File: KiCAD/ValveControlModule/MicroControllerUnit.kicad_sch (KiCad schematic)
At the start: 5 parts, among them U1 XIAO-RP2040-DIP

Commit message: 電源，RS485の仕様を確定
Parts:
- H1, H2, H3, H4: footprint MountingHole:MountingHole_4.3mm_M4_Pad_TopBottom -> MountingHole:MountingHole_3.2mm_M3_Pad_TopBottom
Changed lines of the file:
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@@
 			)
 		)
-		(property "Footprint" "MountingHole:MountingHole_4.3mm_M4_Pad_TopBottom"
+		(property "Footprint" "MountingHole:MountingHole_3.2mm_M3_Pad_TopBottom"
 			(at 190.5 39.37 0)
 			(effects
@@
 			)
 		)
-		(property "Footprint" "MountingHole:MountingHole_4.3mm_M4_Pad_TopBottom"
+		(property "Footprint" "MountingHole:MountingHole_3.2mm_M3_Pad_TopBottom"
 			(at 114.3 39.37 0)
 			(effects
@@
 			)
 		)
-		(property "Footprint" "MountingHole:MountingHole_4.3mm_M4_Pad_TopBottom"
+		(property "Footprint" "MountingHole:MountingHole_3.2mm_M3_Pad_TopBottom"
 			(at 139.7 39.37 0)
 			(effects
@@
 			)
 		)
-		(property "Footprint" "MountingHole:MountingHole_4.3mm_M4_Pad_TopBottom"
+		(property "Footprint" "MountingHole:MountingHole_3.2mm_M3_Pad_TopBottom"
 			(at 165.1 39.37 0)
 			(effects

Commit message: 基本的な機能が完成
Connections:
- no-connect marks 0 -> 1
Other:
- note added: "内部の回路にパスコンあるため省略"
- moved on the sheet: H1, H2, H3, H4, U1

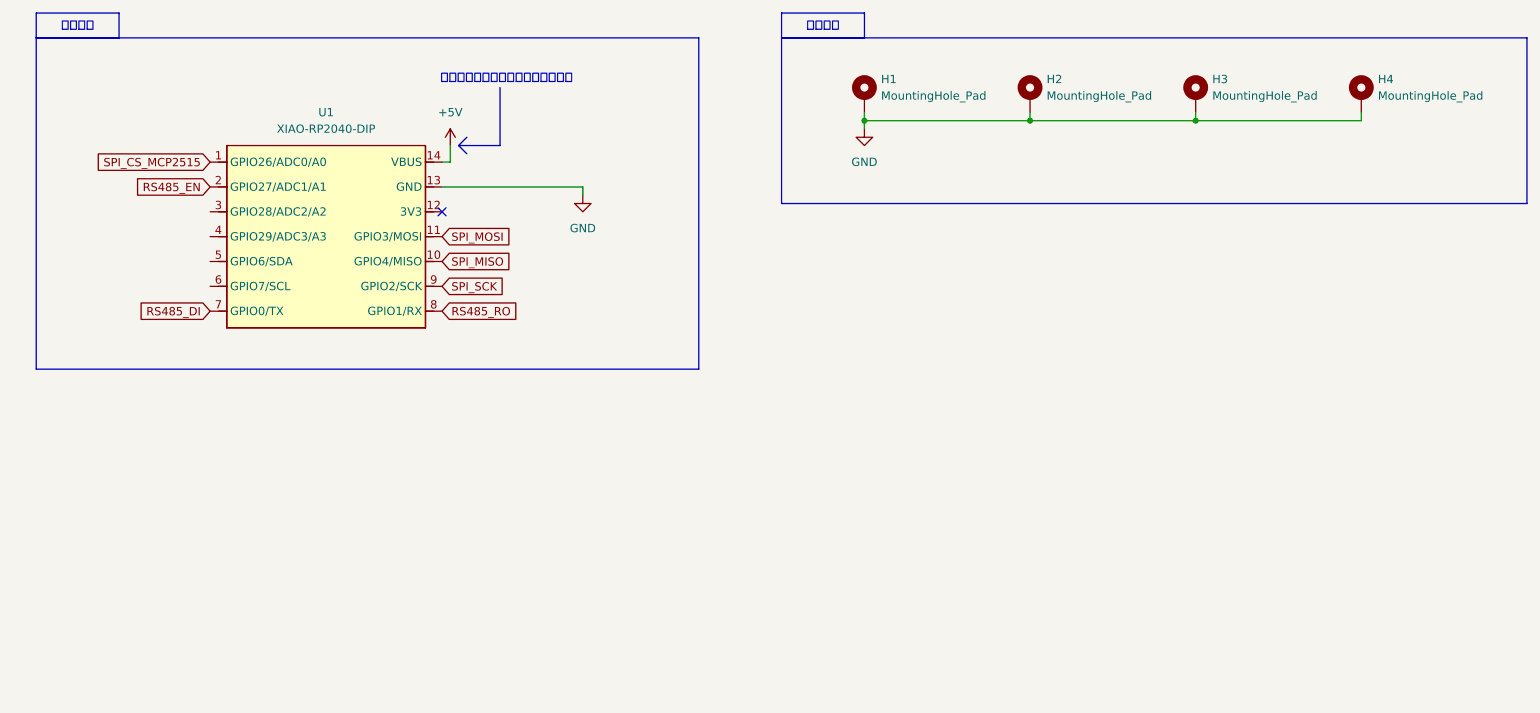
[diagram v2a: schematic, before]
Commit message: 取り付け穴位置を更新
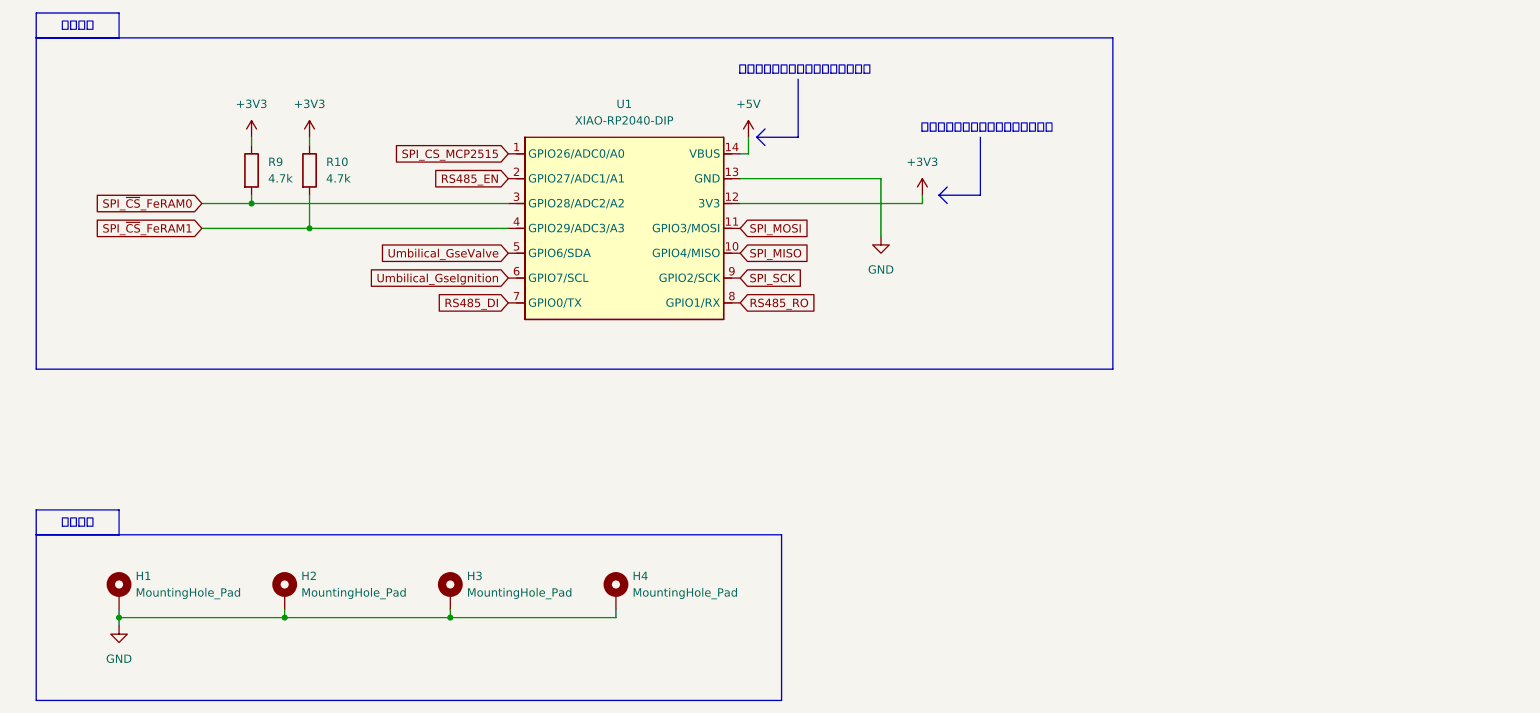
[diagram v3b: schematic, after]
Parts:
- added R10, R9: 4.7k, Resistor_SMD:R_0603_1608Metric_Pad0.98x0.95mm_HandSolder, symbol Device:R
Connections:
- net +3V3: now reaches U1.12 (3V3)
- net +3V3: now also R10.1, R9.1
- net SPI_~{CS}_FeRAM0: now reaches U1.3 (GPIO28/ADC2/A2)
- net SPI_~{CS}_FeRAM0: now also R9.2
- net SPI_~{CS}_FeRAM1: now reaches U1.4 (GPIO29/ADC3/A3)
- net SPI_~{CS}_FeRAM1: now also R10.2
- net Umbilical_GseValve: now reaches U1.5 (GPIO6/SDA)
- net Umbilical_GseIgnition: now reaches U1.6 (GPIO7/SCL)
- no-connect marks 1 -> 0
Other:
- moved on the sheet: H1, H2, H3, H4, U1

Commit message: Build-2完成．発注．
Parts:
- removed R10: 4.7k, Resistor_SMD:R_0603_1608Metric_Pad0.98x0.95mm_HandSolder, symbol Device:R
- H1, H2, H3, H4: symbol Mechanical:MountingHole_Pad -> Mechanical:MountingHole; now in the parts list
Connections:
- net GND: no longer H1.1, H2.1, H3.1, H4.1
- net SPI_~{CS}_FeRAM1 renamed ServoPower_EN
